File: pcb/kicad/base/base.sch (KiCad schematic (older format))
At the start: 40 parts, among them P1 J-Link SWD, P2 SMA, P3 Power Source, P4 USB Micro B, P5 Button, P6 Button, P7 Button, P8 Button, P9 Button, U1 SAMB11G18A-edit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

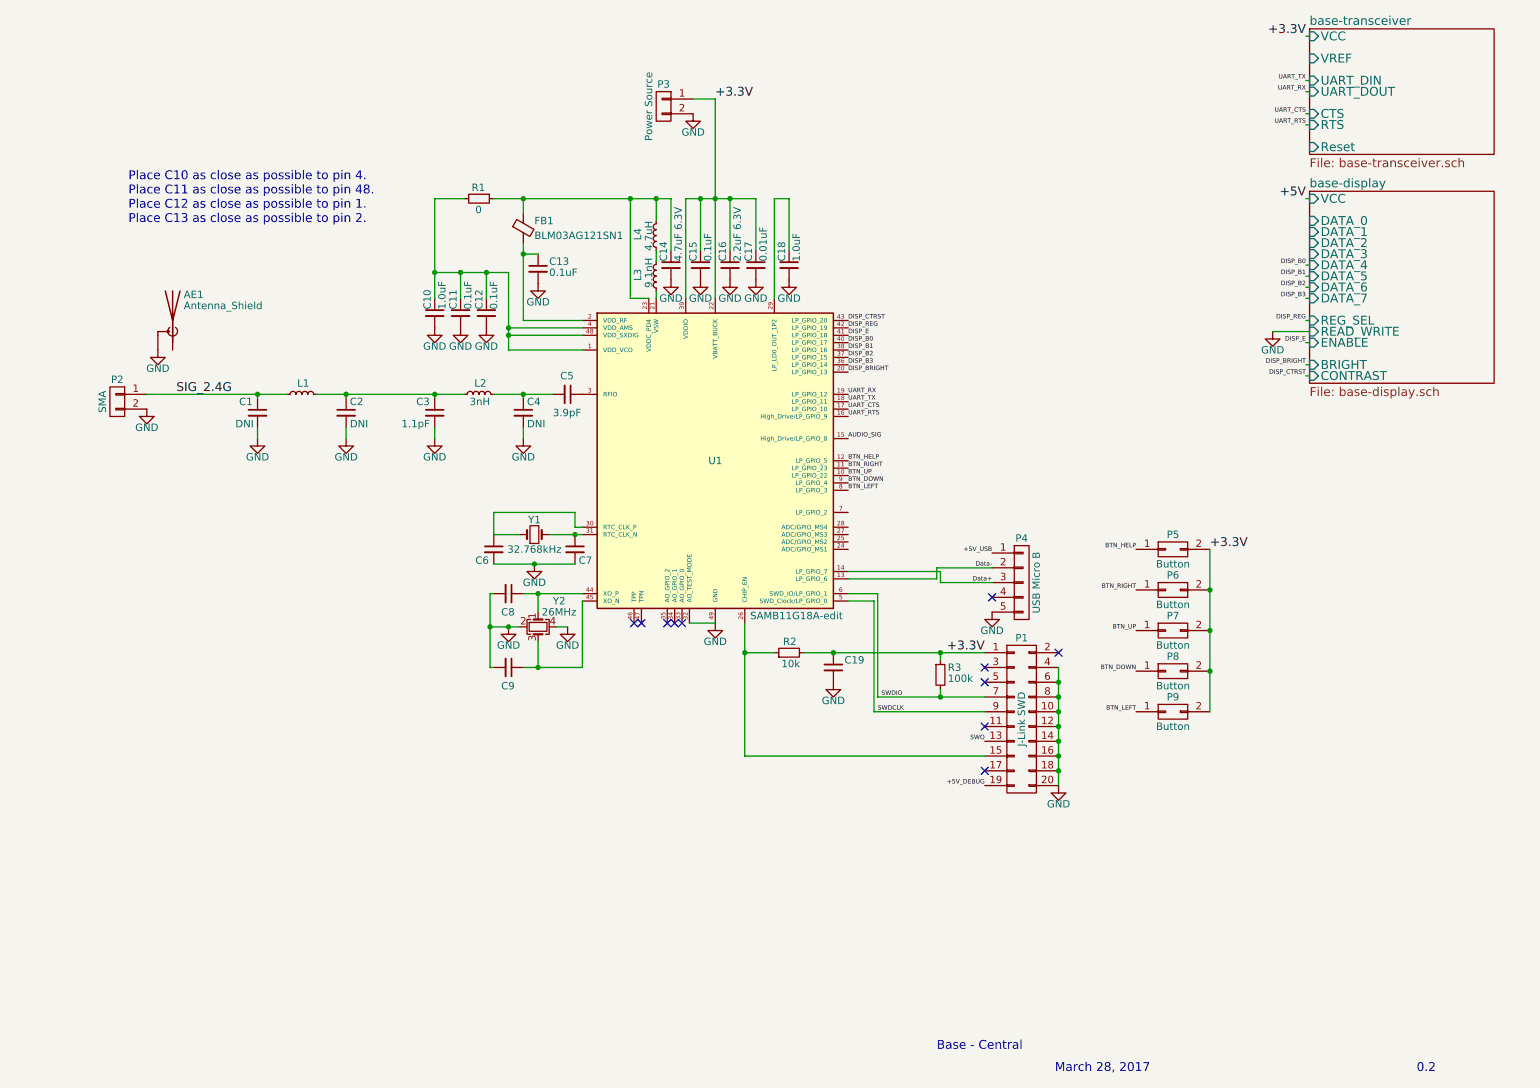
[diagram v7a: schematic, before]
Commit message: Add power traces throughout board
Power is almost fully distributed to the entire board. All signal traces
have been connected. Copper pours still need to removed from the
RF region. The ferrite bead should also be moved.
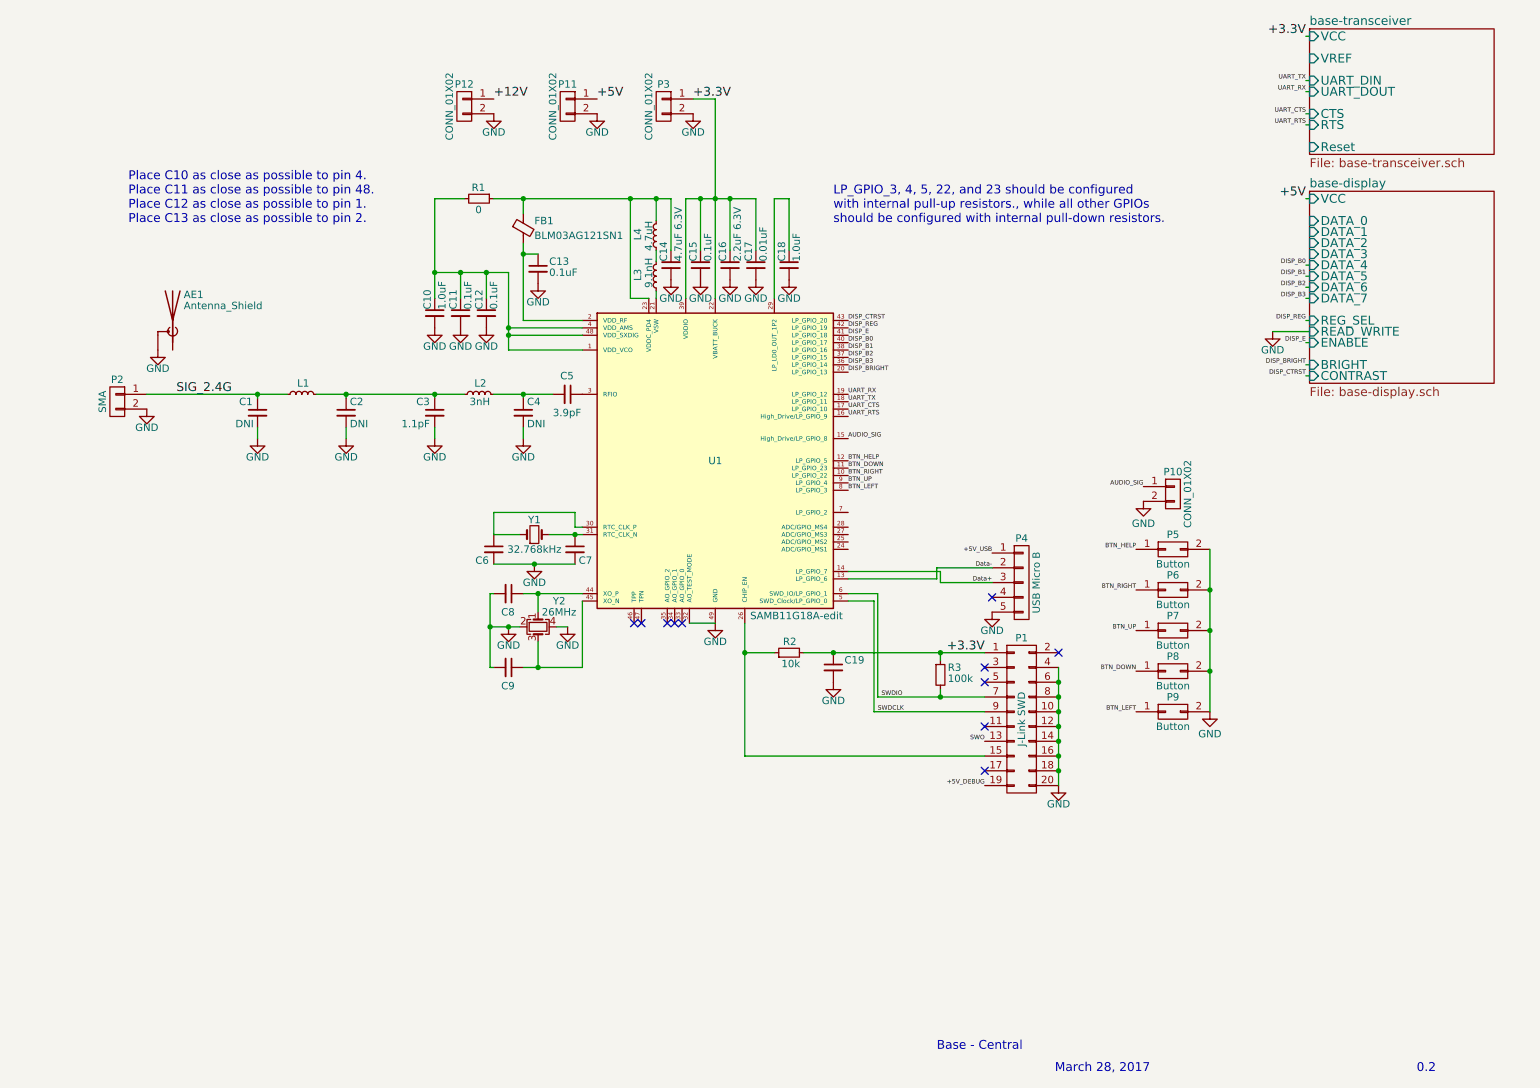
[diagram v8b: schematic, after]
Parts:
- added P10, P11, P12: CONN_01X02, Misc:Socket_Strip_Straight_1x02_Pitch2.54mm_Drill0.64mm, symbol CONN_01X02
- P3: value Power Source -> CONN_01X02
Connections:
- net +3.3V: no longer P5.2 (P2), P6.2 (P2), P7.2 (P2), P8.2 (P2), P9.2 (P2)
- net +5V: now also P11.1 (P1)
- net AUDIO_SIG: now also P10.1 (P1)
- net BTN_DOWN: now also U1.11 (LP_GPIO_23); no longer U1.9 (LP_GPIO_4)
- net BTN_RIGHT: now also U1.10 (LP_GPIO_22); no longer U1.11 (LP_GPIO_23)
- net BTN_UP: now also U1.9 (LP_GPIO_4); no longer U1.10 (LP_GPIO_22)
- net GND: now also P5.2 (P2), P6.2 (P2), P7.2 (P2), P8.2 (P2), P9.2 (P2), P10.2 (P2), P11.2 (P2), P12.2 (P2)
- new net +12V: P12.1 (P1)
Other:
- note added: "LP_GPIO_3, 4, 5, 22, and 23 should be configured\nwith internal pull-up resistors., while all other GPIOs\nshould be configured with internal pull-down resistors."
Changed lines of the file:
@@
 	1    0    0    -1
 $EndComp
-Text Label 5850 1050 0    60   ~ 0
+Text Label 5700 1050 0    60   ~ 0
 +3.3V
 Text Label 2200 3050 0    60   ~ 0
@@
 P 5500 1100
 F 0 "P3" H 5500 1250 50  0000 C CNN
-F 1 "Power Source" V 5600 1100 50  0000 C CNN
+F 1 "CONN_01X02" V 5600 1100 50  0000 C CNN
 F 2 "Misc:Socket_Strip_Straight_1x02_Pitch2.54mm_Drill0.64mm" H 5500 1100 50  0001 C CNN
 F 3 "" H 5500 1100 50  0000 C CNN
@@
 	1    0    0    -1
 $EndComp
-Text Label 9200 4100 0    60   ~ 0
-+3.3V
 Text Label 6750 2550 0    30   ~ 0
 DISP_CTRST
@@
 Text Label 6750 3500 0    30   ~ 0
 BTN_HELP
+Text Label 6750 3600 0    30   ~ 0
+BTN_RIGHT
+Text Label 6750 3650 0    30   ~ 0
+BTN_UP
 Text Label 6750 3550 0    30   ~ 0
-BTN_RIGHT
-Text Label 6750 3600 0    30   ~ 0
-BTN_UP
-Text Label 6750 3650 0    30   ~ 0
 BTN_DOWN
 Text Label 6750 3700 0    30   ~ 0
 BTN_LEFT
+$Comp
+L CONN_01X02 P10
+U 1 1 58E94ECD
+P 8950 3725
+F 0 "P10" H 8950 3875 50  0000 C CNN
+F 1 "CONN_01X02" V 9050 3725 50  0000 C CNN
+F 2 "Misc:Socket_Strip_Straight_1x02_Pitch2.54mm_Drill0.64mm" H 8950 3725 50  0001 C CNN
+F 3 "" H 8950 3725 50  0000 C CNN
+	1    8950 3725
+	1    0    0    -1
+$EndComp
+$Comp
+L GND #PWR025
+U 1 1 58E97BCF
+P 8750 3775
+F 0 "#PWR025" H 8750 3525 50  0001 C CNN
+F 1 "GND" H 8750 3625 50  0000 C CNN
+F 2 "" H 8750 3775 50  0000 C CNN
+F 3 "" H 8750 3775 50  0000 C CNN
+	1    8750 3775
+	1    0    0    -1
+$EndComp
+Text Label 8750 3675 2    30   ~ 0
+AUDIO_SIG
+$Comp
+L GND #PWR026
+U 1 1 58EA125A
+P 9200 5200
+F 0 "#PWR026" H 9200 4950 50  0001 C CNN
+F 1 "GND" H 9200 5050 50  0000 C CNN
+F 2 "" H 9200 5200 50  0000 C CNN
+F 3 "" H 9200 5200 50  0000 C CNN
+	1    9200 5200
+	1    0    0    -1
+$EndComp
+Text Notes 6650 1900 0    60   ~ 0
+LP_GPIO_3, 4, 5, 22, and 23 should be configured\nwith internal pull-up resistors., while all other GPIOs\nshould be configured with internal pull-down resistors.
+$Comp
+L CONN_01X02 P11
+U 1 1 58EB82D6
+P 4850 1100
+F 0 "P11" H 4850 1250 50  0000 C CNN
+F 1 "CONN_01X02" V 4950 1100 50  0000 C CNN
+F 2 "Misc:Socket_Strip_Straight_1x02_Pitch2.54mm_Drill0.64mm" H 4850 1100 50  0001 C CNN
+F 3 "" H 4850 1100 50  0000 C CNN
+	1    4850 1100
+	-1   0    0    -1
+$EndComp
+$Comp
+L GND #PWR027
+U 1 1 58EB898D
+P 5050 1150
+F 0 "#PWR027" H 5050 900 50  0001 C CNN
+F 1 "GND" H 5050 1025 50  0000 C CNN
+F 2 "" H 5050 1150 50  0000 C CNN
+F 3 "" H 5050 1150 50  0000 C CNN
+	1    5050 1150
+	1    0    0    -1
+$EndComp
+Text Label 5050 1050 0    60   ~ 0
++5V
+$Comp
+L CONN_01X02 P12
+U 1 1 58EBD0A2
+P 4150 1100
+F 0 "P12" H 4150 1250 50  0000 C CNN
+F 1 "CONN_01X02" V 4250 1100 50  0000 C CNN
+F 2 "Misc:Socket_Strip_Straight_1x02_Pitch2.54mm_Drill0.64mm" H 4150 1100 50  0001 C CNN
+F 3 "" H 4150 1100 50  0000 C CNN
+	1    4150 1100
+	-1   0    0    -1
+$EndComp
+Text Label 4350 1050 0    60   ~ 0
++12V
+$Comp
+L GND #PWR028
+U 1 1 58EBD46E
+P 4350 1150
+F 0 "#PWR028" H 4350 900 50  0001 C CNN
+F 1 "GND" H 4350 1025 50  0000 C CNN
+F 2 "" H 4350 1150 50  0000 C CNN
+F 3 "" H 4350 1150 50  0000 C CNN
+	1    4350 1150
+	1    0    0    -1
+$EndComp
 $EndSCHEMATC
